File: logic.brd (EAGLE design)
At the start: 37.4 x 32.5 mm, 9 parts, among them CON1 PINHEAD_1X10-2, CON2 PINHEAD_1X10-2, CON4 PINHEAD_1X02-2, CON5 PINHEAD_1X02-2, CON6 PINHEAD_1X02-2, CON7 PINHEAD_1X07-2

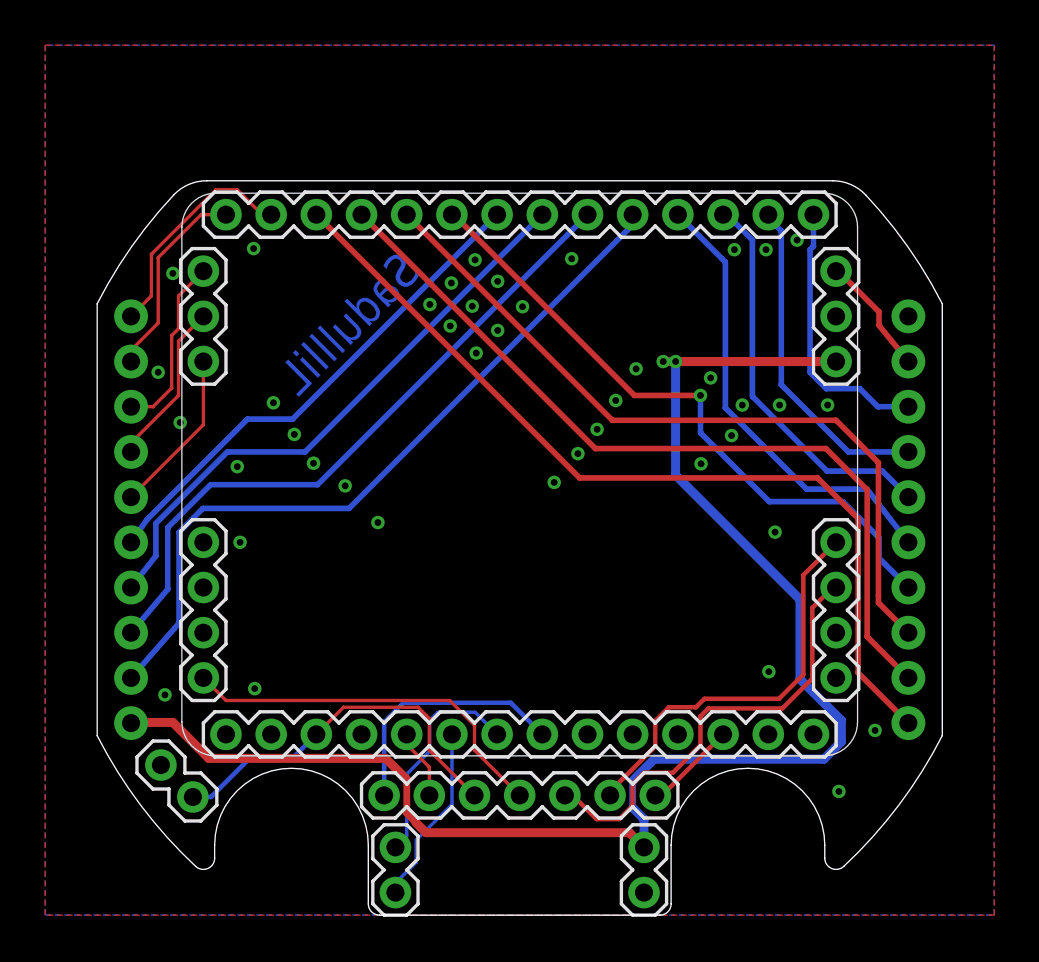
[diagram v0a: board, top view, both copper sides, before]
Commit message: pinout fixes
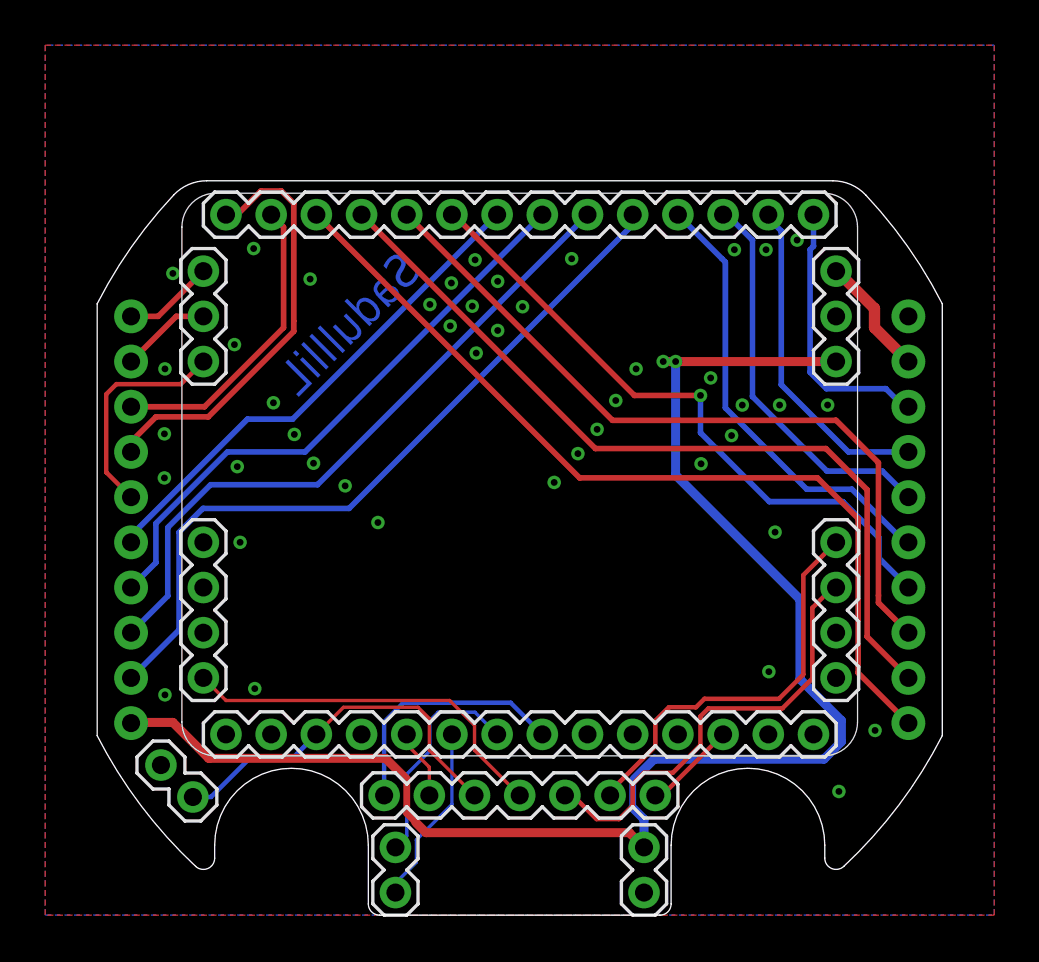
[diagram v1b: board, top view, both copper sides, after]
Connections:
- removed net N$1: CON2.3, MODULE2.18
- removed net N$2: CON2.2, MODULE2.17
- removed net N$3: CON2.1, MODULE2.16
- removed net N$4: CON2.4, MODULE2.19
- removed net N$5: CON1.1, MODULE2.15
- new net PHASE_A_CURRENT_SHUNT_N: CON2.3, MODULE2.16
- new net PHASE_A_CURRENT_SHUNT_P: CON2.4, MODULE2.17
- new net PHASE_B_CURRENT_SHUNT_N: CON2.1, MODULE2.18
- new net PHASE_B_CURRENT_SHUNT_P: CON2.2, MODULE2.19
- new net PHASE_B_GND: CON2.6, MODULE2.11
- net PHASE_B: now also CON2.8, MODULE2.9; no longer CON1.3, MODULE2.13
- net PHASE_B_GATE_HIGH: now also CON2.9, MODULE2.8; no longer CON1.4, MODULE2.12
- net PHASE_B_GATE_LOW: now also CON2.7, MODULE2.10; no longer CON1.2, MODULE2.14
- net PHASE_C: now also CON1.3, MODULE2.13; no longer CON2.8, MODULE2.9
- net PHASE_C_GATE_HIGH: now also CON1.4, MODULE2.12; no longer CON2.9, MODULE2.8
- net PHASE_C_GATE_LOW: now also CON1.2, MODULE2.14; no longer CON2.7, MODULE2.10
- net PHASE_C_GND: now also CON1.1, MODULE2.15; no longer CON2.6, MODULE2.11
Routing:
- net N$5: track 39.5 -> 0.00 mm
- net PHASE_B_GND: track 0.00 -> 22.4 mm
- net PHASE_A_CURRENT_SHUNT_P: track 0.00 -> 19.0 mm
- net PHASE_C_GND: track 22.3 -> 39.5 mm
- net PHASE_A_CURRENT_SHUNT_N: track 0.00 -> 13.4 mm
- net PHASE_C_GATE_LOW: track 26.0 -> 36.5 mm
- net PHASE_B_GATE_LOW: track 36.5 -> 26.1 mm
- net N$3: track 10.1 -> 0.00 mm
- net N$2: track 8.88 -> 0.00 mm
- net N$1: track 7.90 -> 0.00 mm
- net N$4: track 7.33 -> 0.00 mm
- net PHASE_B_GATE_HIGH: track 28.5 -> 33.5 mm, vias 1 -> 0
- net PHASE_C_GATE_HIGH: track 33.4 -> 28.5 mm, vias 0 -> 1
- net PHASE_B_CURRENT_SHUNT_P: track 0.00 -> 4.03 mm
- net PHASE_B_CURRENT_SHUNT_N: track 0.00 -> 4.03 mm
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
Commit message: updates
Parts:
- renumbered MODULE2 to MODULE1

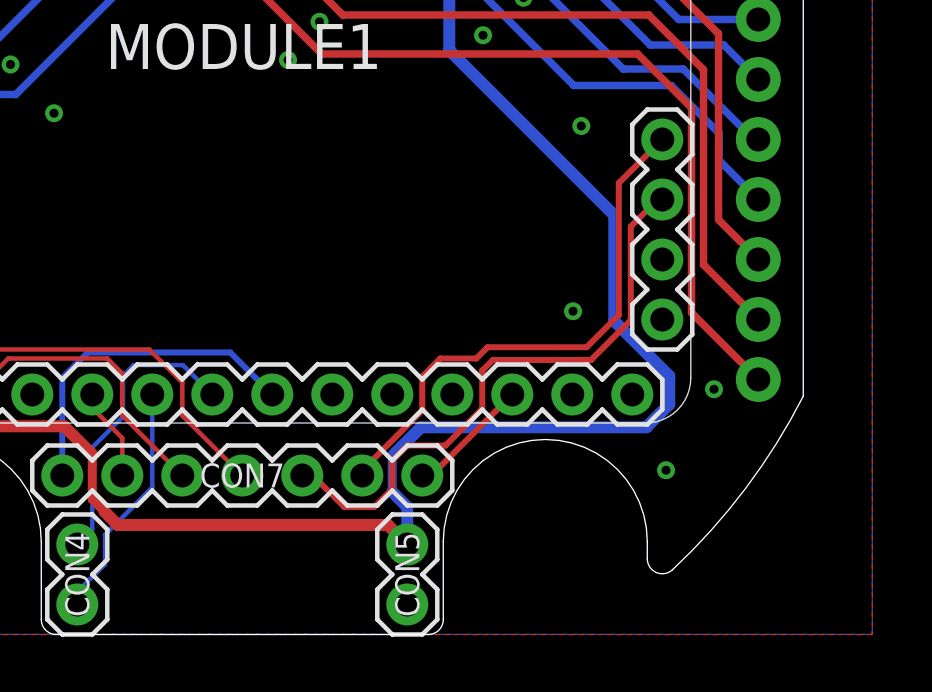
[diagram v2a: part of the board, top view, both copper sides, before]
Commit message: Logic board update.
Thermistor connection moved to other side of the PCB
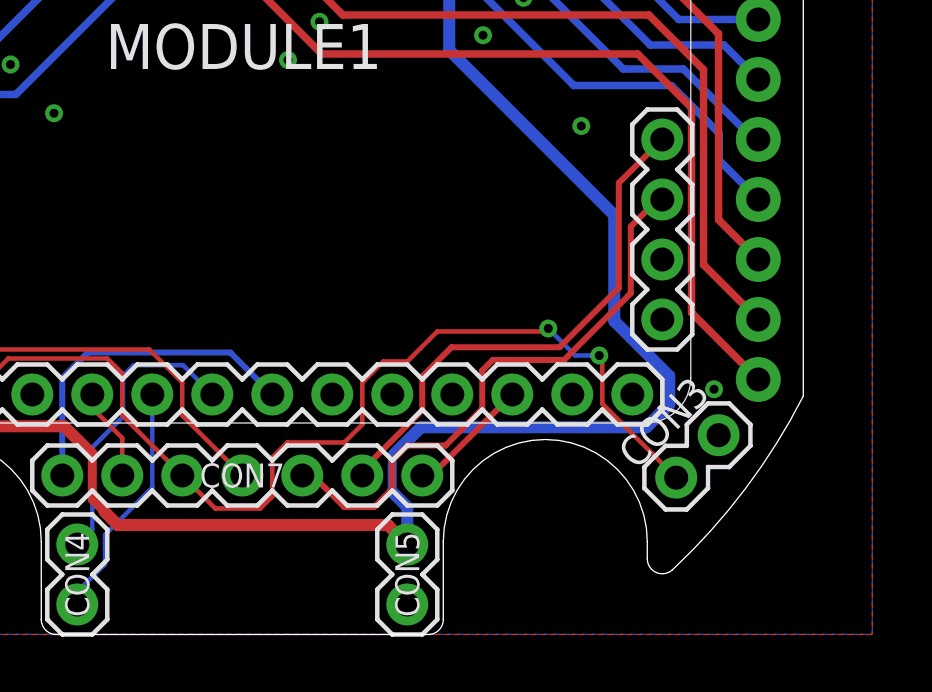
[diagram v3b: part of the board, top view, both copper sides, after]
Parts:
- added CON3: PINHEAD_1X02-2, pinhead:1X02-PTH-2
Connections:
- net GND: now also CON3.2
- net GPIO1: now also CON3.1
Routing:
- net GPIO1: track 16.5 -> 40.5 mm, vias 0 -> 2
- net CAN1_TX: track 18.0 -> 17.5 mm
- net CAN1_RX: track 19.8 -> 19.3 mm
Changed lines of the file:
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@@
 <setting verticaltext="up"/>
 </settings>
-<grid distance="0.05" unitdist="mm" unit="mm" style="lines" multiple="1" display="no" altdistance="5" altunitdist="mil" altunit="mil"/>
+<grid distance="0.1" unitdist="mm" unit="mm" style="lines" multiple="1" display="no" altdistance="5" altunitdist="mil" altunit="mil"/>
 <layers>
 <layer number="1" name="Top" color="4" fill="1" visible="yes" active="yes"/>
@@
 <layer number="14" name="Route14" color="22" fill="1" visible="no" active="no"/>
 <layer number="15" name="Route15" color="23" fill="1" visible="no" active="no"/>
-<layer number="16" name="Bottom" color="1" fill="1" visible="no" active="yes"/>
+<layer number="16" name="Bottom" color="1" fill="1" visible="yes" active="yes"/>
 <layer number="17" name="Pads" color="2" fill="1" visible="yes" active="yes"/>
 <layer number="18" name="Vias" color="2" fill="1" visible="yes" active="yes"/>
@@
 <layer number="20" name="Dimension" color="24" fill="1" visible="yes" active="yes"/>
 <layer number="21" name="tPlace" color="7" fill="1" visible="yes" active="yes"/>
-<layer number="22" name="bPlace" color="7" fill="1" visible="no" active="yes"/>
+<layer number="22" name="bPlace" color="7" fill="1" visible="yes" active="yes"/>
 <layer number="23" name="tOrigins" color="15" fill="1" visible="yes" active="yes"/>
-<layer number="24" name="bOrigins" color="15" fill="1" visible="no" active="yes"/>
+<layer number="24" name="bOrigins" color="15" fill="1" visible="yes" active="yes"/>
 <layer number="25" name="tNames" color="7" fill="1" visible="yes" active="yes"/>
-<layer number="26" name="bNames" color="7" fill="1" visible="no" active="yes"/>
+<layer number="26" name="bNames" color="7" fill="1" visible="yes" active="yes"/>
 <layer number="27" name="tValues" color="7" fill="1" visible="no" active="yes"/>
 <layer number="28" name="bValues" color="7" fill="1" visible="no" active="yes"/>
@@
 <layer number="46" name="Milling" color="3" fill="1" visible="no" active="yes"/>
 <layer number="47" name="Measures" color="7" fill="1" visible="no" active="yes"/>
-<layer number="48" name="Document" color="7" fill="1" visible="no" active="yes"/>
+<layer number="48" name="Document" color="7" fill="1" visible="yes" active="yes"/>
 <layer number="49" name="Reference" color="7" fill="1" visible="no" active="yes"/>
 <layer number="50" name="dxf" color="7" fill="1" visible="no" active="no"/>
 <layer number="51" name="tDocu" color="7" fill="1" visible="yes" active="yes"/>
-<layer number="52" name="bDocu" color="7" fill="1" visible="no" active="yes"/>
+<layer number="52" name="bDocu" color="7" fill="1" visible="yes" active="yes"/>
 <layer number="53" name="tGND_GNDA" color="7" fill="9" visible="no" active="no"/>
 <layer number="54" name="bGND_GNDA" color="1" fill="9" visible="no" active="no"/>
@@
 <wire x1="6.7" y1="-14.4" x2="13.5" y2="-14.4" width="0.01" layer="20" curve="-180" locked="yes"/>
 <wire x1="13.5" y1="-14.4" x2="13.5" y2="-14.975" width="0.01" layer="20" locked="yes"/>
+<circle x="0" y="0" radius="21" width="0.01" layer="48"/>
+<circle x="0" y="0" radius="20" width="0.01" layer="48"/>
+<circle x="0" y="0" radius="20.5" width="0.01" layer="48"/>
 </plain>
 <attributes>
 </attributes>
 <variantdefs>
-<variantdef name="BASIC" current="yes"/>
+<variantdef name="BASIC"/>
 </variantdefs>
 <classes>
@@
 <attribute name="NAME" x="5.5" y="-15.5" size="0.8" layer="25" font="vector" ratio="15" rot="R270" align="center"/>
 </element>
-<element name="CON6" library="pinhead" library_urn="urn:adsk.eagle:library:2540341" package="1X02-PTH-2" package3d_urn="urn:adsk.eagle:package:6503394/3" value="PINHEAD_1X02-2" x="-15.171" y="-11.564" populate="no" smashed="yes" rot="R135"/>
+<element name="CON6" library="pinhead" library_urn="urn:adsk.eagle:library:2540341" package="1X02-PTH-2" package3d_urn="urn:adsk.eagle:package:6503394/3" value="PINHEAD_1X02-2" x="-15.171" y="-11.564" smashed="yes" rot="R135"/>
 <element name="CON7" library="pinhead" library_urn="urn:adsk.eagle:library:2540341" package="1X07-PTH-2" package3d_urn="urn:adsk.eagle:package:2540391/3" value="PINHEAD_1X07-2" x="0" y="-12.2" smashed="yes">
 <attribute name="NAME" x="0" y="-12.2" size="0.8" layer="25" font="vector" ratio="15" align="center"/>
 </element>
 <element name="U$2" library="logo" library_urn="urn:adsk.eagle:library:6668987" package="OSHW-10.5X11.5" value="" x="5.5" y="-7" smashed="yes" rot="MR0"/>
+<element name="CON3" library="pinhead" library_urn="urn:adsk.eagle:library:2540341" package="1X02-PTH-2" package3d_urn="urn:adsk.eagle:package:6503394/3" value="PINHEAD_1X02-2" x="15.171" y="-11.564" smashed="yes" rot="R45">
+<attribute name="NAME" x="14.03963125" y="-10.432628125" size="1" layer="25" font="vector" ratio="15" rot="R45" align="center"/>
+</element>
 </elements>
 <signals>
@@
 <via x="-6.275" y="-0.125" extent="1-16" drill="0.3" diameter="0.6"/>
 <via x="-11.725" y="-7.475" extent="1-16" drill="0.3" diameter="0.6"/>
-<via x="11.025" y="-6.725" extent="1-16" drill="0.3" diameter="0.6"/>
 <via x="11.3" y="-0.55" extent="1-16" drill="0.3" diameter="0.6"/>
 <via x="9.85" y="5.075" extent="1-16" drill="0.3" diameter="0.6"/>
@@
 <contactref element="CON6" pad="2"/>
 <contactref element="CON5" pad="2"/>
-<via x="14.125" y="-12.025" extent="1-16" drill="0.3" diameter="0.6"/>
 <via x="15.725" y="-9.325" extent="1-16" drill="0.3" diameter="0.6"/>
 <via x="8.025" y="2.475" extent="1-16" drill="0.3" diameter="0.6"/>
@@
 <via x="-15.725" y="3.8" extent="1-16" drill="0.3" diameter="0.6"/>
 <via x="-15.725" y="1.85" extent="1-16" drill="0.3" diameter="0.6"/>
+<contactref element="CON3" pad="2"/>
 </signal>
 <signal name="VDC" class="1">
@@
 <signal name="CAN1_TX">
 <contactref element="MODULE1" pad="42"/>
-<wire x1="12.55" y1="-6.85" x2="11.475" y2="-7.925" width="0.2" layer="1"/>
-<wire x1="12.55" y1="-6.85" x2="12.55" y2="-2.45" width="0.2" layer="1"/>
+<wire x1="12.55" y1="-5.95" x2="10.575" y2="-7.925" width="0.2" layer="1"/>
+<wire x1="12.55" y1="-5.95" x2="12.55" y2="-2.45" width="0.2" layer="1"/>
 <wire x1="12.55" y1="-2.45" x2="14" y2="-1" width="0.2" layer="1"/>
-<wire x1="11.475" y1="-7.925" x2="8.175" y2="-7.925" width="0.2" layer="1"/>
-<wire x1="7.8" y1="-8.3" x2="6.6" y2="-8.3" width="0.2" layer="1"/>
-<wire x1="6.6" y1="-8.3" x2="6" y2="-8.9" width="0.2" layer="1"/>
-<wire x1="8.175" y1="-7.925" x2="7.8" y2="-8.3" width="0.2" layer="1"/>
+<wire x1="10.575" y1="-7.925" x2="6.975" y2="-7.925" width="0.2" layer="1"/>
+<wire x1="6.975" y1="-7.925" x2="6" y2="-8.9" width="0.2" layer="1"/>
 <wire x1="6" y1="-8.9" x2="6" y2="-10.0281" width="0.2" layer="1"/>
 <contactref element="CON7" pad="6"/>
@@
 <wire x1="14" y1="-3" x2="13.85" y2="-3" width="0.2" layer="1"/>
 <wire x1="13.85" y1="-3" x2="12.95" y2="-3.9" width="0.2" layer="1"/>
-<wire x1="12.95" y1="-3.9" x2="12.95" y2="-7.025" width="0.2" layer="1"/>
-<wire x1="12.95" y1="-7.025" x2="11.625" y2="-8.35" width="0.2" layer="1"/>
-<wire x1="11.625" y1="-8.35" x2="8.35" y2="-8.35" width="0.2" layer="1"/>
+<wire x1="12.95" y1="-3.9" x2="12.95" y2="-6.125" width="0.2" layer="1"/>
+<wire x1="12.95" y1="-6.125" x2="10.725" y2="-8.35" width="0.2" layer="1"/>
+<wire x1="10.725" y1="-8.35" x2="8.35" y2="-8.35" width="0.2" layer="1"/>
 <wire x1="8.35" y1="-8.35" x2="8" y2="-8.7" width="0.2" layer="1"/>
 <wire x1="8" y1="-8.7" x2="8" y2="-9.9751" width="0.2" layer="1"/>
@@
 <wire x1="-4" y1="-8.8" x2="-4.5" y2="-8.3" width="0.15" layer="1"/>
 <wire x1="-4.5" y1="-8.3" x2="-7.8" y2="-8.3" width="0.15" layer="1"/>
+<contactref element="CON3" pad="1"/>
+<wire x1="-2" y1="-12.2" x2="-0.9" y2="-13.3" width="0.1524" layer="1"/>
+<wire x1="-0.9" y1="-13.3" x2="0.6" y2="-13.3" width="0.1524" layer="1"/>
+<wire x1="0.6" y1="-13.3" x2="1" y2="-12.9" width="0.1524" layer="1"/>
+<wire x1="1" y1="-12.9" x2="1" y2="-11.6" width="0.1524" layer="1"/>
+<wire x1="1" y1="-11.6" x2="1.5" y2="-11.1" width="0.1524" layer="1"/>
+<wire x1="1.5" y1="-11.1" x2="3.4" y2="-11.1" width="0.1524" layer="1"/>
+<wire x1="3.4" y1="-11.1" x2="4" y2="-10.5" width="0.1524" layer="1"/>
+<wire x1="4" y1="-10.5" x2="4" y2="-9.1" width="0.1524" layer="1"/>
+<wire x1="4" y1="-9.1" x2="4.7" y2="-8.4" width="0.1524" layer="1"/>
+<wire x1="4.7" y1="-8.4" x2="5.5" y2="-8.4" width="0.1524" layer="1"/>
+<wire x1="5.5" y1="-8.4" x2="6.5" y2="-7.4" width="0.1524" layer="1"/>
+<wire x1="10.1" y1="-7.4" x2="10.2" y2="-7.3" width="0.1524" layer="1"/>
+<via x="10.2" y="-7.3" extent="1-16" drill="0.3" diameter="0.6"/>
+<wire x1="6.5" y1="-7.4" x2="10.1" y2="-7.4" width="0.1524" layer="1"/>
+<wire x1="10.2" y1="-7.3" x2="11.1" y2="-8.2" width="0.1524" layer="16"/>
+<wire x1="11.1" y1="-8.2" x2="11.9" y2="-8.2" width="0.1524" layer="16"/>
+<via x="11.9" y="-8.2" extent="1-16" drill="0.3" diameter="0.6"/>
+<wire x1="11.9" y1="-8.2" x2="12" y2="-8.3" width="0.1524" layer="1"/>
+<wire x1="12.61635" y1="-10.4262" x2="12.618984375" y2="-10.4262" width="0.1524" layer="1"/>
+<wire x1="12.618984375" y1="-10.4262" x2="14.463890625" y2="-12.27110625" width="0.1524" layer="1"/>
+<wire x1="12" y1="-9.80985" x2="12.61635" y2="-10.4262" width="0.1524" layer="1"/>
+<wire x1="12" y1="-8.3" x2="12" y2="-9.80985" width="0.1524" layer="1"/>
 </signal>
 <signal name="GPIO2">
